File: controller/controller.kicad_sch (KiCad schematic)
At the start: 4 parts, among them J1 Conn_01x02_Socket, J2 Conn_01x02_Socket, SW1 SW_Push_Dual, U1 Pico

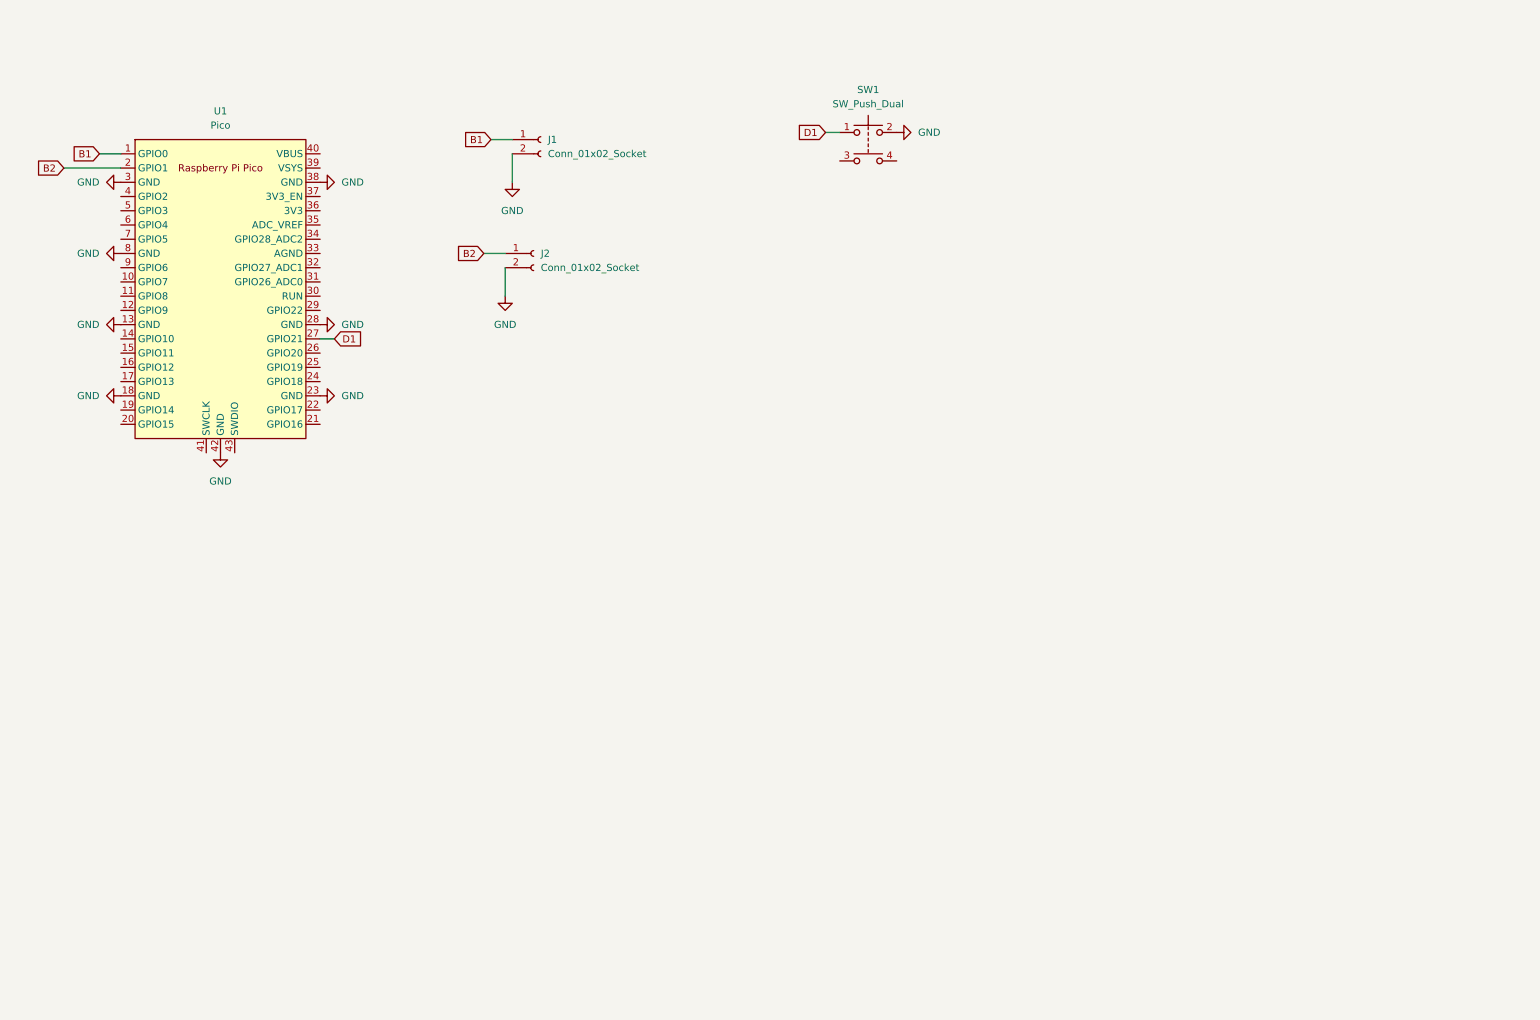
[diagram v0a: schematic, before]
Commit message: Splitting dpad out into its own board
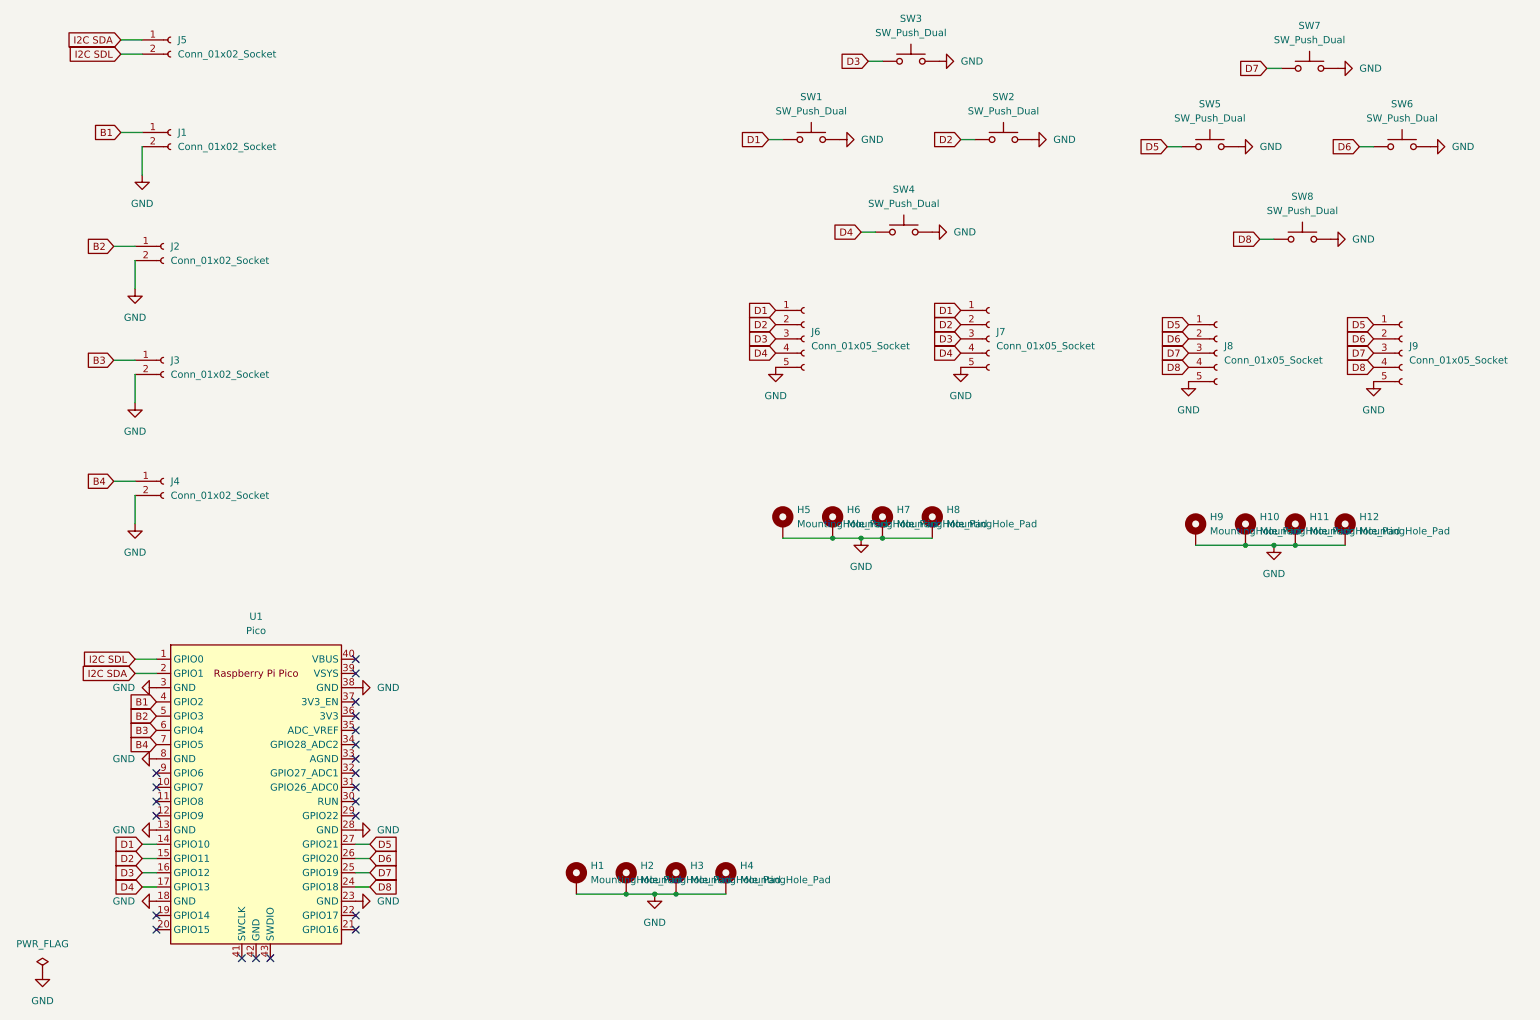
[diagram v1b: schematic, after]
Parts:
- added H1, H10, H11, H12, H2, H3, H4, H5, H6, H7, H8, H9: MountingHole_Pad, MountingHole:MountingHole_3.2mm_M3_Pad, symbol Mechanical:MountingHole_Pad
- added J3, J4, J5: Conn_01x02_Socket, Connector_JST:JST_XH_B2B-XH-AM_1x02_P2.50mm_Vertical, symbol Connector:Conn_01x02_Socket
- added J6, J7, J8, J9: Conn_01x05_Socket, Connector_PinHeader_1.00mm:PinHeader_1x05_P1.00mm_Vertical, symbol Connector:Conn_01x05_Socket
- added SW2, SW3, SW4, SW5, SW6, SW7, SW8: SW_Push_Dual, Button_Switch_THT:SW_PUSH-12mm, symbol Switch:SW_Push
- J1: footprint Button_Switch_THT:SW_TH_Tactile_Omron_B3F-10xx -> Connector_JST:JST_XH_B2B-XH-AM_1x02_P2.50mm_Vertical
- SW1: footprint Button_Switch_THT:SW_TH_Tactile_Omron_B3F-10xx -> Button_Switch_THT:SW_PUSH-12mm; symbol Switch:SW_Push_Dual -> Switch:SW_Push
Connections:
- net B1: now also U1.4 (GPIO2); no longer U1.1 (GPIO0)
- net B2: now also U1.5 (GPIO3); no longer U1.2 (GPIO1)
- net D1: now also U1.14 (GPIO10), J6.1 (Pin_1), J7.1 (Pin_1); no longer U1.27 (GPIO21)
- net GND: now also H1.1, H10.1, H11.1, H12.1, H2.1, H3.1, H4.1, H5.1, H6.1, H7.1, H8.1, H9.1, J3.2 (Pin_2), J4.2 (Pin_2), J6.5 (Pin_5), J7.5 (Pin_5), J8.5 (Pin_5), J9.5 (Pin_5), SW2.2, SW3.2, SW4.2, SW5.2, SW6.2, SW7.2, SW8.2; no longer U1.42 (GND)
- net D2: now reaches U1.15 (GPIO11)
- net D2: now also J6.2 (Pin_2), J7.2 (Pin_2), SW2.1
- net D3: now reaches U1.16 (GPIO12)
- net D3: now also J6.3 (Pin_3), J7.3 (Pin_3), SW3.1
- net D4: now reaches U1.17 (GPIO13)
- net D4: now also J6.4 (Pin_4), J7.4 (Pin_4), SW4.1
- net D8: now reaches U1.24 (GPIO18)
- net D8: now also J8.4 (Pin_4), J9.4 (Pin_4), SW8.1
- net D7: now reaches U1.25 (GPIO19)
- net D7: now also J8.3 (Pin_3), J9.3 (Pin_3), SW7.1
- net D6: now reaches U1.26 (GPIO20)
- net D6: now also J8.2 (Pin_2), J9.2 (Pin_2), SW6.1
- net B3: now reaches U1.6 (GPIO4)
- net B3: now also J3.1 (Pin_1)
- net B4: now reaches U1.7 (GPIO5)
- net B4: now also J4.1 (Pin_1)
- new net D5: J8.1 (Pin_1), J9.1 (Pin_1), SW5.1, U1.27 (GPIO21)
- new net I2C SDA: J5.1 (Pin_1), U1.2 (GPIO1)
- new net I2C SDL: J5.2 (Pin_2), U1.1 (GPIO0)
- no-connect marks 0 -> 22
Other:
- moved on the sheet: J1, J2, U1
